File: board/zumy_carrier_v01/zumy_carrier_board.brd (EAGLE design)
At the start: 90 x 60 mm, 28 parts, among them IC1 SN74AUP2G17, IC2 SN74AUP2G17, J1 ODROID_POWER, J2 BATT_POWER, SW1 500SSP1S1M6QEA

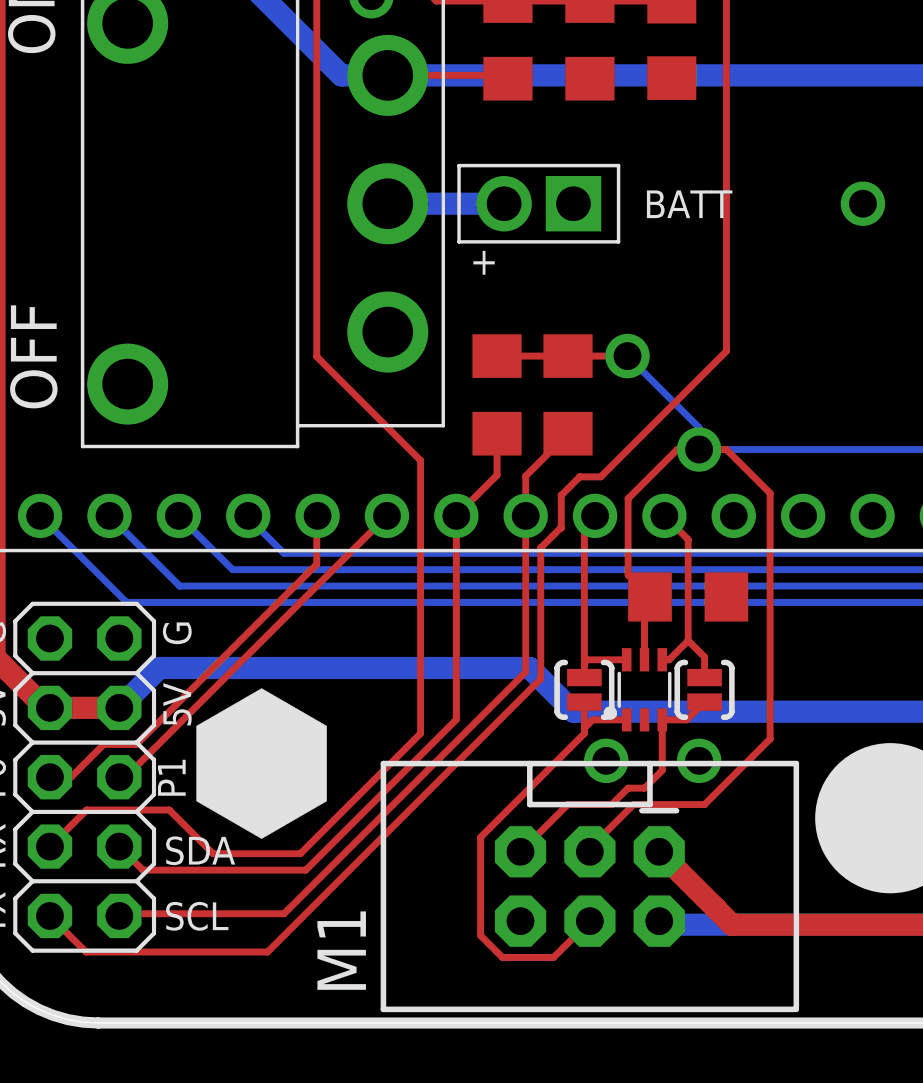
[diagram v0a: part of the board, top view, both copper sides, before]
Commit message: Adding voltage monitor breakout board.
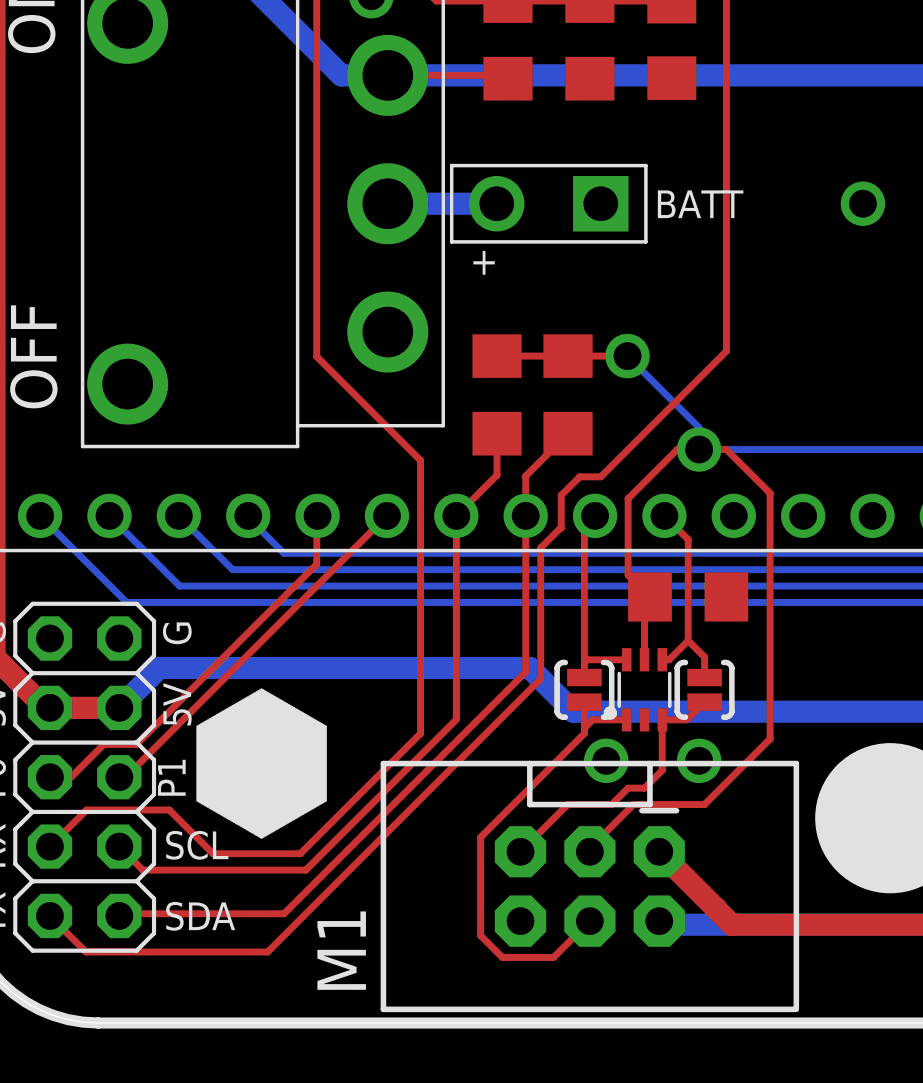
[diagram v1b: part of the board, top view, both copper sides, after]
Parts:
- moved J2 1.00 mm to (-21.6, 0.00)
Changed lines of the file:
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@@
 <text x="36" y="13.8" size="1.6764" layer="21" font="vector" ratio="18" rot="SR270">Rev E</text>
 <text x="-43.2" y="-3.6" size="1.6764" layer="21" font="vector" ratio="18" rot="R270">OFF</text>
-<text x="-20.034825" y="-0.0188375" size="1.016" layer="21" font="vector" ratio="18" rot="R180" align="center-right">BATT</text>
+<text x="-19.634825" y="-0.0188375" size="1.016" layer="21" font="vector" ratio="18" rot="R180" align="center-right">BATT</text>
 <text x="-41.6" y="5.4" size="1.6764" layer="21" font="vector" ratio="18" rot="R90">ON</text>
 <wire x1="40" y1="-30" x2="-40" y2="-30" width="0.4064" layer="21"/>
@@
 <text x="-43.4" y="-21.8" size="1.016" layer="21" font="vector" ratio="20" rot="R90">P0</text>
 <text x="-36.8" y="-21.8" size="1.016" layer="21" font="vector" ratio="20" rot="R90">P1</text>
-<text x="-37.6" y="-24.2" size="1.016" layer="21" font="vector" ratio="20">SDA</text>
-<text x="-37.6" y="-26.6" size="1.016" layer="21" font="vector" ratio="20">SCL</text>
+<text x="-37.6" y="-26.6" size="1.016" layer="21" font="vector" ratio="20">SDA</text>
+<text x="-37.6" y="-24" size="1.016" layer="21" font="vector" ratio="20">SCL</text>
 <text x="-43.4" y="-24.4" size="1.016" layer="21" font="vector" ratio="20" rot="R90">RX</text>
 <text x="-43.4" y="-26.8" size="1.016" layer="21" font="vector" ratio="20" rot="R90">TX</text>
@@
 <element name="J1" library="zumy" package="ODOIRD_PWR" value="ODROID_POWER" x="37" y="-26.4" smashed="yes"/>
 <element name="SW1" library="zumy" package="500SSP1S1M6QEA_SWITCH" value="500SSP1S1M6QEA" x="-29.4" y="0" smashed="yes" rot="R90"/>
-<element name="J2" library="zumy" package="BATT_POWER" value="BATT_POWER" x="-22.6" y="0" smashed="yes" rot="R180"/>
+<element name="J2" library="zumy" package="BATT_POWER" value="BATT_POWER" x="-21.6" y="0" smashed="yes" rot="R180"/>
 <element name="U$4" library="zumy" package="STANDOFF_POSITION" value="" x="42" y="-20.5" rot="R90"/>
 <element name="M1" library="SparkFun-Connectors" package="2X3-SHROUDED" value="" x="-22" y="-25" smashed="yes" rot="R270">
@@
 <contactref element="J2" pad="PWR"/>
 <contactref element="SW1" pad="2"/>
-<wire x1="-25.14" y1="0" x2="-29.4" y2="0" width="0.8128" layer="16"/>
+<wire x1="-25.41" y1="0" x2="-29.4" y2="0" width="0.8128" layer="16"/>
 </signal>
 <signal name="V+">

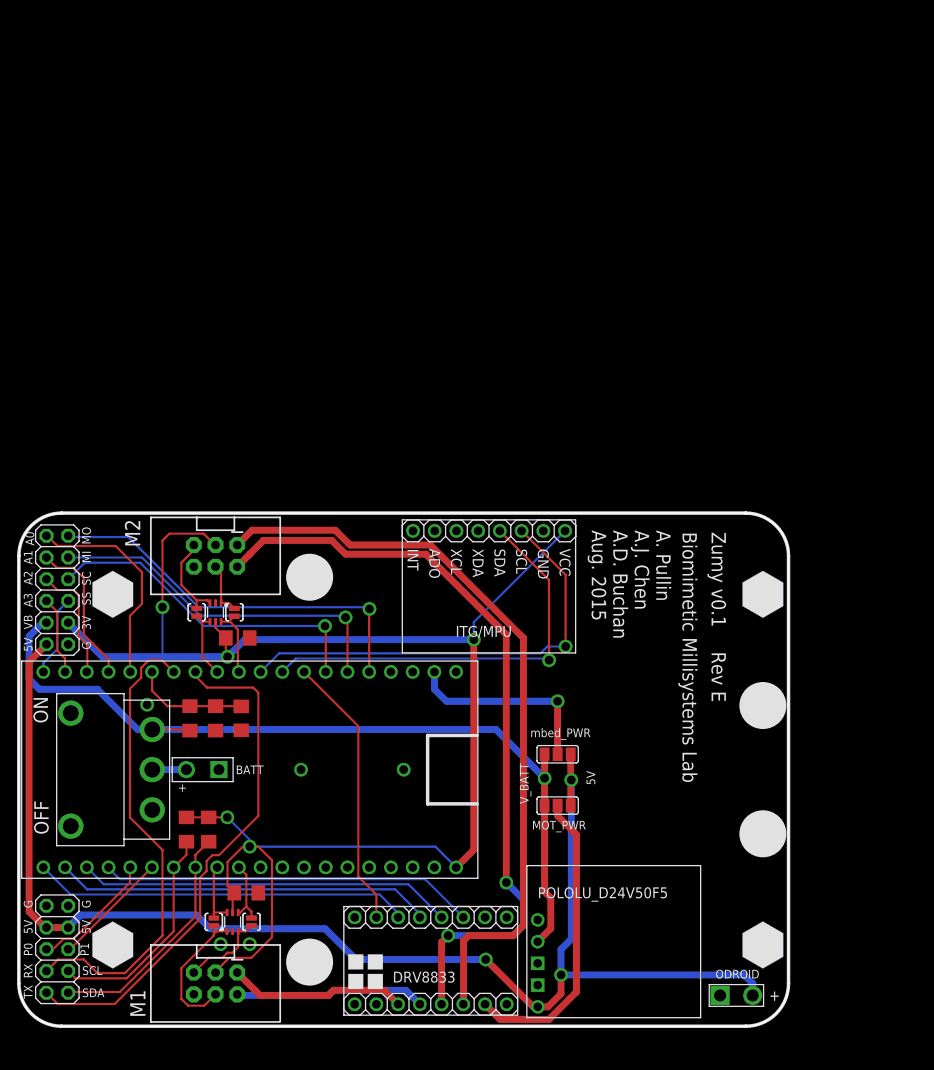
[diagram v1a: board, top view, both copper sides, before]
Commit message: Finishing touches for Rev. F. Moved voltage regulator to not conflict with mbed USB cable. Added support post holes for accelerometer and voltage regulator. Increased drill for battery and odroid power. Added hint lines for surface mount components.
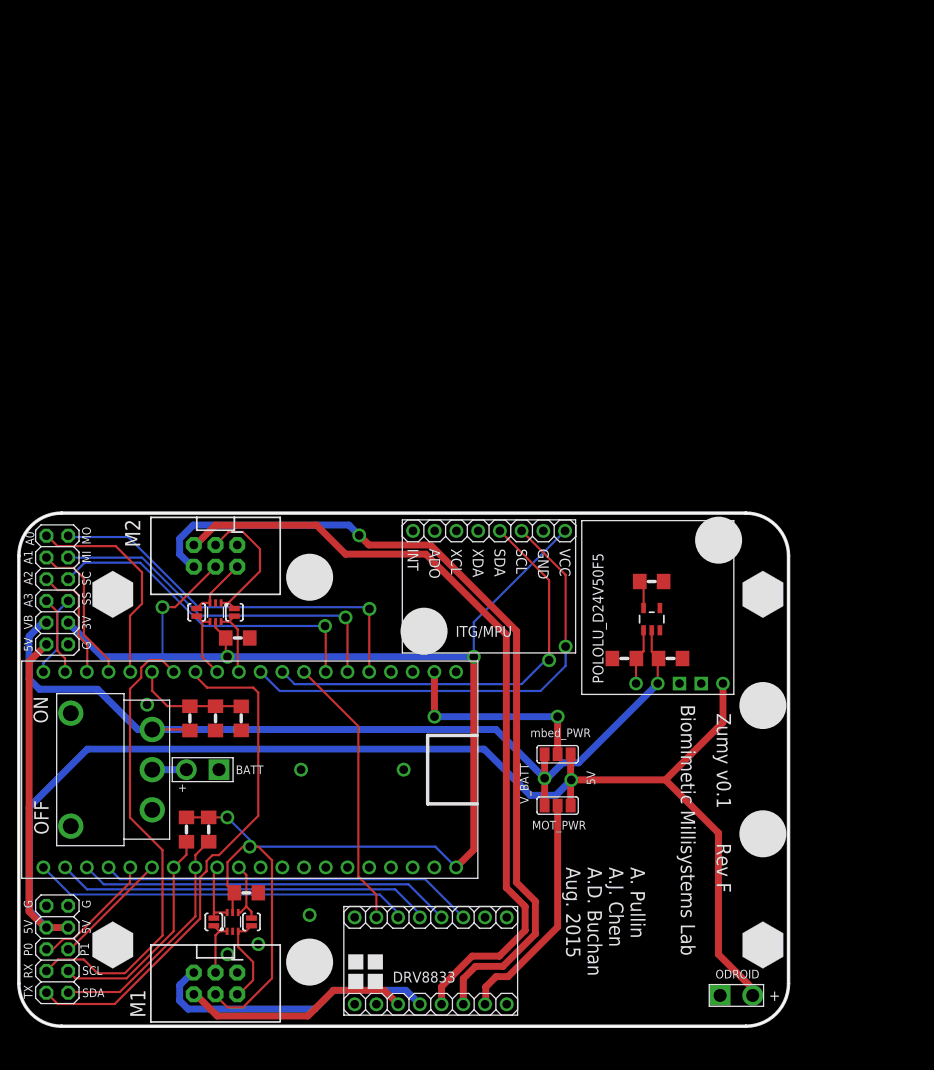
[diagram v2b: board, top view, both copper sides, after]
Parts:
- added C4, C6: 0.1uF, rcl:C1206
- added C5: 1uF, rcl:C1206
- added U$2: BD5260G, zumy:SOT23-5
- moved U$5 44.9 mm to (38.6, 8.80), turned to 90 degrees
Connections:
- new net N$4: C6.1, U$2.1, U$5.EN
- new net N$6: C5.1, U$2.5
- net +3V3: now also M1.4, M2.4; no longer M1.3, M2.3
- net GND: now also C4.2, C5.2, C6.2, M1.1, M2.1, U$2.3; no longer M1.6, M2.6
- net M1_EA: now also M1.3; no longer M1.4
- net M1_EB: now also M1.2; no longer M1.5
- net M1_OUT1: now also M1.6; no longer M1.1
- net M1_OUT2: now also M1.5; no longer M1.2
- net M2_EA: now also M2.3; no longer M2.4
- net M2_EB: now also M2.2; no longer M2.5
- net M2_OUT1: now also M2.6; no longer M2.1
- net M2_OUT2: now also M2.5; no longer M2.2
- net V+: now also C4.1, U$2.2
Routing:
- net +5V: track 156.5 -> 182.1 mm, vias 3 -> 1
- net M1_OUT2: track 22.3 -> 34.2 mm
- net M2_OUT1: track 88.2 -> 99.2 mm, vias 0 -> 1
- net M2_EA: track 6.32 -> 16.3 mm
- net M1_EA: track 16.7 -> 6.84 mm
- net N$3: track 35.5 -> 27.6 mm
- net V+: track 100.1 -> 107.6 mm
- net N$4: track 0.00 -> 6.59 mm
- net M1_OUT1: track 20.8 -> 26.9 mm
- net N$6: track 0.00 -> 3.29 mm
- net MPU_SCL: track 52.5 -> 55.7 mm
- net M2_OUT2: track 89.8 -> 92.9 mm, vias 2 -> 0
- net M2_EB: track 10.4 -> 7.37 mm
- net +3V3: track 184.9 -> 182.2 mm
- net MPU_SDA: track 49.4 -> 50.7 mm
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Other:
- board text added: "Rev F"
- board text removed: "Rev E"

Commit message: Starting to shuffle board around for ODROID-C2 update.
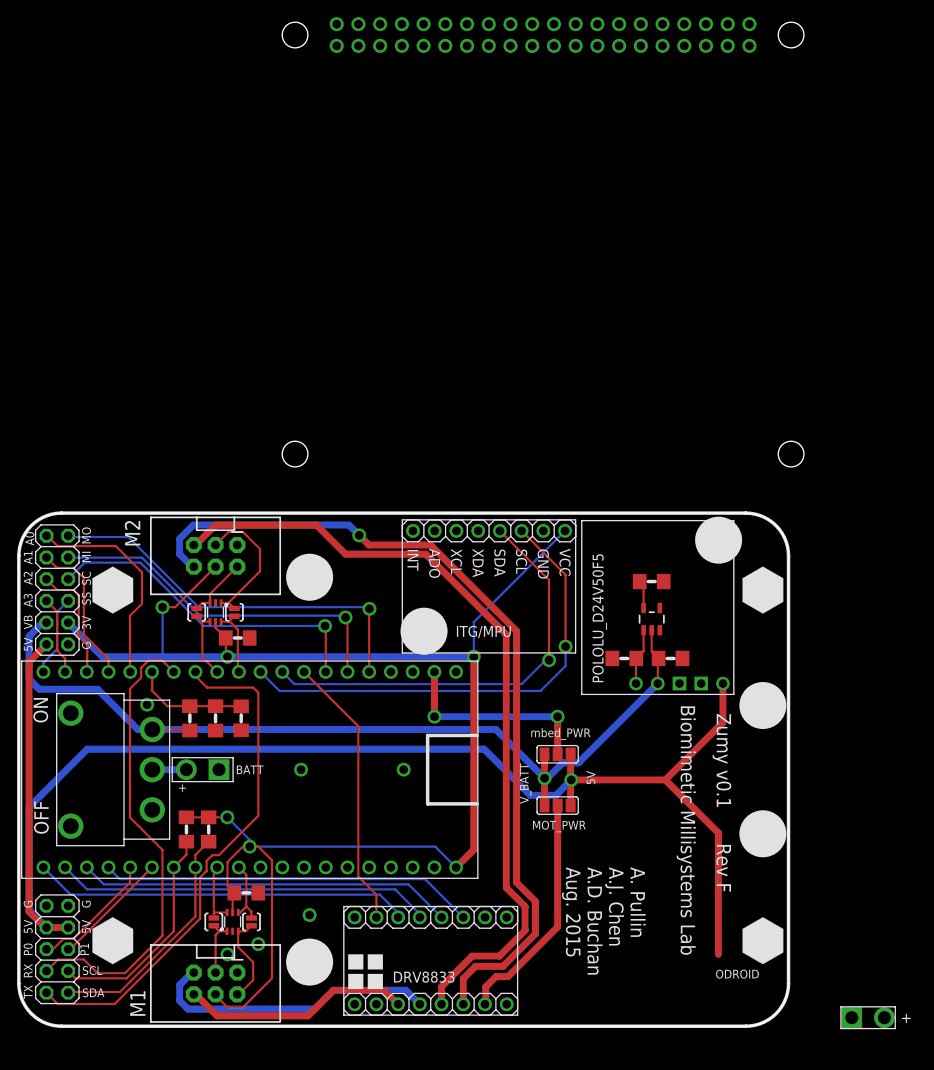
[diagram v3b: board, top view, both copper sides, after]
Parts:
- added U$3: ZUMY_LOGO, zumy:ZUMY_LOGO_SILK
- added U$6: ODROID-C2, zumy:ODROID-C2-BOARD
- U$4: device zumy:STANDOFF_POSITION -> zumy:ODROID_U3_MOUNTING
- moved J1 15.6 mm to (52.4, -29.0)
- moved U$4 0.50 mm to (42.0, -20.0)
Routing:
- net +5V: track 182.1 -> 175.6 mm
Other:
- board text removed: "ZUMY"
